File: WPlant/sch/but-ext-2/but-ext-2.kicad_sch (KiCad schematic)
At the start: 14 parts, among them J1 eInk, J4 But2, SW1 SW_Push, SW2 SW_Push, SW3 SW_Push, SW4 SW_Push, U2 SMTSOM365BTR, U3 SMTSOM365BTR

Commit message: Added PCB templates for 2 boards around eInk display
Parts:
- added H2: MountingHole, MountingHole:MountingHole_3mm, symbol Mechanical:MountingHole
- H1: footprint (none) -> MountingHole:MountingHole_3mm
- J1: footprint (none) -> Connector_PinHeader_2.54mm:PinHeader_1x08_P2.54mm_Vertical
- J4: footprint (none) -> Connector_PinHeader_2.54mm:PinHeader_2x06_P2.54mm_Vertical
- SW1, SW2, SW3, SW4: footprint (none) -> Button_Switch_THT:SW_PUSH_6mm_H13mm
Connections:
- net GND: now reaches J1.1 (Pin_1), J4.4 (Pin_4), SW1.1, SW2.1, SW3.1, SW4.1
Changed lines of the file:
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@@
+		)
+	)
+	(label "GND"
+		(at 127 123.19 0)
+		(effects
+			(font
+				(size 1.27 1.27)
+			)
+			(justify left bottom)
 		)
 	)
@@
 			)
 		)
-		(property "Footprint" ""
+		(property "Footprint" "Button_Switch_THT:SW_PUSH_6mm_H13mm"
 			(at 101.6 83.82 0)
 			(hide yes)
@@
 				(path "/44ee3f62-13f6-4236-babe-1fe6b14f82df"
 					(reference "SW3")
+					(unit 1)
+				)
+			)
+		)
+	)
+	(symbol
+		(lib_id "Mechanical:MountingHole")
+		(at 240.03 115.57 0)
+		(unit 1)
+		(body_style 1)
+		(exclude_from_sim no)
+		(in_bom no)
+		(on_board yes)
+		(in_pos_files yes)
+		(dnp no)
+		(fields_autoplaced yes)
+		(property "Reference" "H2"
+			(at 242.57 114.2999 0)
+			(show_name no)
+			(do_not_autoplace no)
+			(effects
+				(font
+					(size 1.27 1.27)
+				)
+				(justify left)
+			)
+		)
+		(property "Value" "MountingHole"
+			(at 242.57 116.8399 0)
+			(show_name no)
+			(do_not_autoplace no)
+			(effects
+				(font
+					(size 1.27 1.27)
+				)
+				(justify left)
+			)
+		)
+		(property "Footprint" "MountingHole:MountingHole_3mm"
+			(at 240.03 115.57 0)
+			(hide yes)
+			(show_name no)
+			(do_not_autoplace no)
+			(effects
+				(font
+					(size 1.27 1.27)
+				)
+			)
+		)
+		(property "Datasheet" ""
+			(at 240.03 115.57 0)
+			(hide yes)
+			(show_name no)
+			(do_not_autoplace no)
+			(effects
+				(font
+					(size 1.27 1.27)
+				)
+			)
+		)
+		(property "Description" "Mounting Hole without connection"
+			(at 240.03 115.57 0)
+			(hide yes)
+			(show_name no)
+			(do_not_autoplace no)
+			(effects
+				(font
+					(size 1.27 1.27)
+				)
+			)
+		)
+		(instances
+			(project "but-ext-2"
+				(path "/44ee3f62-13f6-4236-babe-1fe6b14f82df"
+					(reference "H2")
 					(unit 1)
 				)
@@
 			)
 		)
-		(property "Footprint" ""
+		(property "Footprint" "Button_Switch_THT:SW_PUSH_6mm_H13mm"
 			(at 101.6 74.93 0)
 			(hide yes)
@@
 			)
 		)
-		(property "Footprint" ""
+		(property "Footprint" "MountingHole:MountingHole_3mm"
 			(at 240.03 109.22 0)
 			(hide yes)
@@
 			)
 		)
-		(property "Footprint" ""
+		(property "Footprint" "Connector_PinHeader_2.54mm:PinHeader_2x06_P2.54mm_Vertical"
 			(at 207.01 104.14 0)
 			(hide yes)
@@
 			)
 		)
-		(property "Footprint" ""
+		(property "Footprint" "Button_Switch_THT:SW_PUSH_6mm_H13mm"
 			(at 101.6 93.98 0)
 			(hide yes)
@@
 			)
 		)
-		(property "Footprint" ""
+		(property "Footprint" "Button_Switch_THT:SW_PUSH_6mm_H13mm"
 			(at 101.6 66.04 0)
 			(hide yes)
@@
 			)
 		)
-		(property "Footprint" ""
+		(property "Footprint" "Connector_PinHeader_2.54mm:PinHeader_1x08_P2.54mm_Vertical"
 			(at 180.34 106.68 0)
 			(hide yes)

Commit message: One of Buttons PCB roughted
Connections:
- net W2: now also D4.1; no longer D4.2
- net W3: now also D4.2; no longer D4.1
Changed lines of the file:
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@@
+	)
+	(junction
+		(at 139.7 96.52)
+		(diameter 0)
+		(color 0 0 0 0)
 	)
 	(junction
@@
 	)
 	(junction
-		(at 143.51 93.98)
+		(at 135.89 91.44)
 		(diameter 0)
 		(color 0 0 0 0)
@@
 	(junction
 		(at 147.32 86.36)
-		(diameter 0)
-		(color 0 0 0 0)
-	)
-	(junction
-		(at 139.7 96.52)
 		(diameter 0)
 		(color 0 0 0 0)
@@
 	(wire
 		(pts
+			(xy 135.89 91.44) (xy 143.51 91.44)
+		)
+		(stroke
+			(width 0)
+			(type default)
+		)
+	)
+	(wire
+		(pts
 			(xy 90.17 88.9) (xy 96.52 88.9)
 		)
@@
 	(wire
 		(pts
-			(xy 132.08 96.52) (xy 139.7 96.52)
-		)
-		(stroke
-			(width 0)
-			(type default)
-		)
-	)
-	(wire
-		(pts
-			(xy 132.08 101.6) (xy 143.51 101.6)
-		)
-		(stroke
-			(width 0)
-			(type default)
-		)
-	)
-	(wire
-		(pts
-			(xy 143.51 93.98) (xy 143.51 101.6)
+			(xy 139.7 96.52) (xy 139.7 101.6)
+		)
+		(stroke
+			(width 0)
+			(type default)
+		)
+	)
+	(wire
+		(pts
+			(xy 132.08 101.6) (xy 139.7 101.6)
 		)
 		(stroke
@@
 	(wire
 		(pts
+			(xy 135.89 96.52) (xy 135.89 91.44)
+		)
+		(stroke
+			(width 0)
+			(type default)
+		)
+	)
+	(wire
+		(pts
 			(xy 132.08 68.58) (xy 143.51 68.58)
 		)
@@
 	(wire
 		(pts
+			(xy 132.08 96.52) (xy 135.89 96.52)
+		)
+		(stroke
+			(width 0)
+			(type default)
+		)
+	)
+	(wire
+		(pts
 			(xy 185.42 111.76) (xy 201.93 111.76)
 		)
@@
 	(wire
 		(pts
-			(xy 132.08 91.44) (xy 143.51 91.44)
-		)
-		(stroke
+			(xy 132.08 91.44) (xy 135.89 91.44)
+		)
+		(stroke

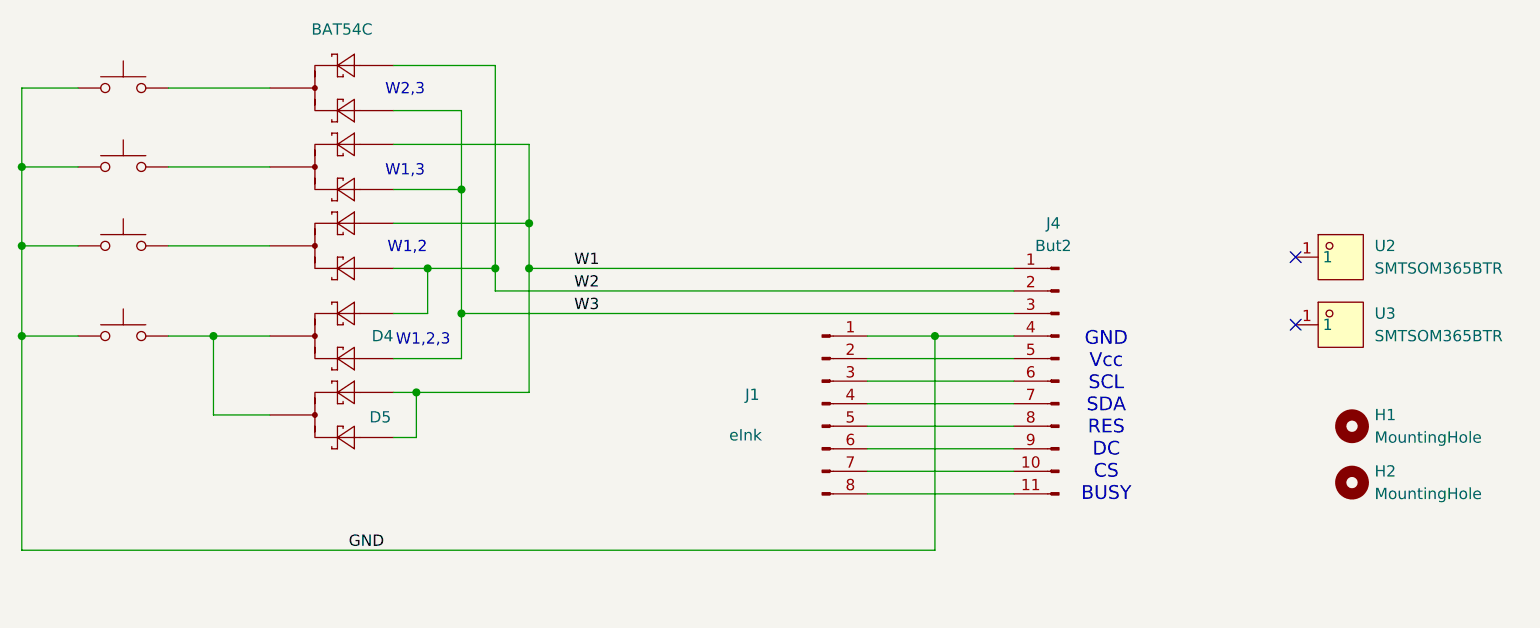
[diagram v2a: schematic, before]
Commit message: Add 3D model of Robots head pole support
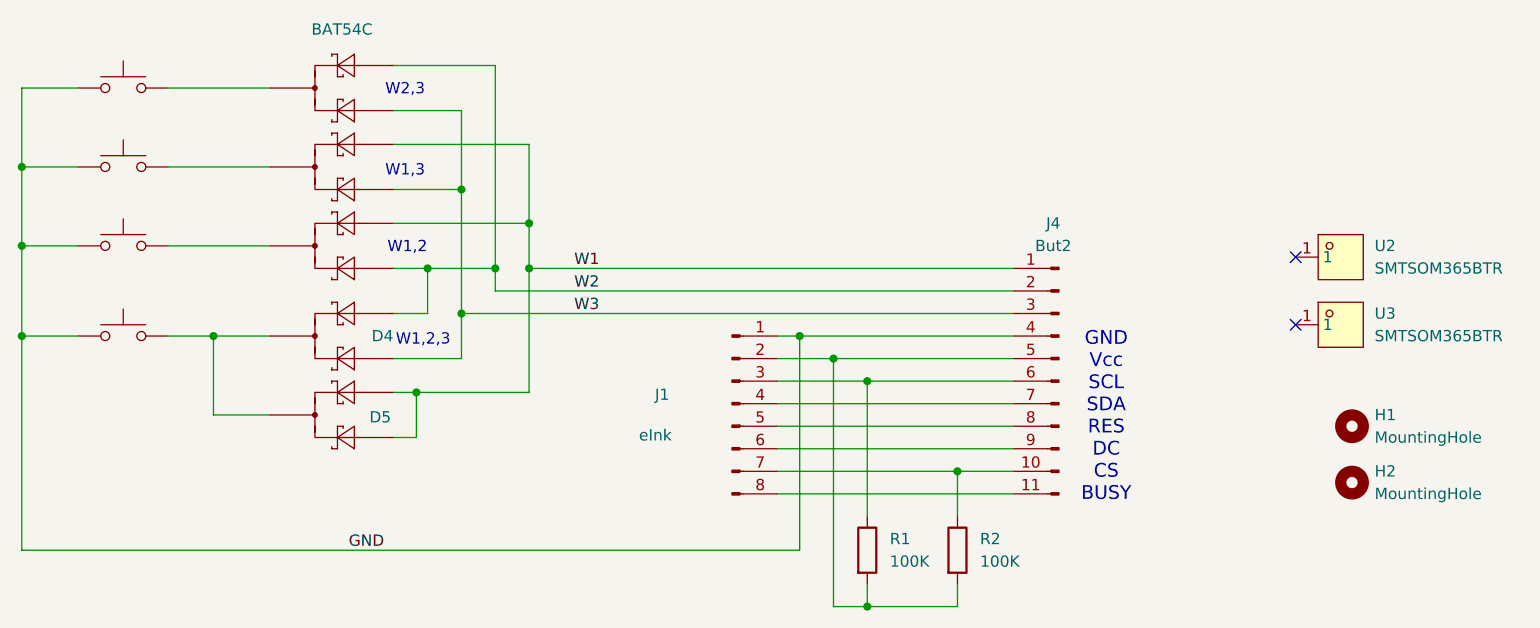
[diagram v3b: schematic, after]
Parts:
- added R1, R2: 100K, Resistor_SMD:R_0603_1608Metric_Pad0.98x0.95mm_HandSolder, symbol Device:R
- U2, U3: footprint easyeda2kicad:SMD_BD5.6-D4.1 -> but:SMD_BD5.6-D4.1
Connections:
- net at J1.7 (Pin_7), J4.10 (Pin_10): now also R2.1
- net at J1.2 (Pin_2), J4.5 (Pin_5): now also R1.2, R2.2
- net at J1.3 (Pin_3), J4.6 (Pin_6): now also R1.1
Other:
- moved on the sheet: J1
